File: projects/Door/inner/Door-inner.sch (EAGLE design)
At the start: 25 parts, among them IC1 7815T, IC2 317T, J3 LCD_4PIN, X1 POWERSUPPLY_DC21MMX, Y1 16MHz

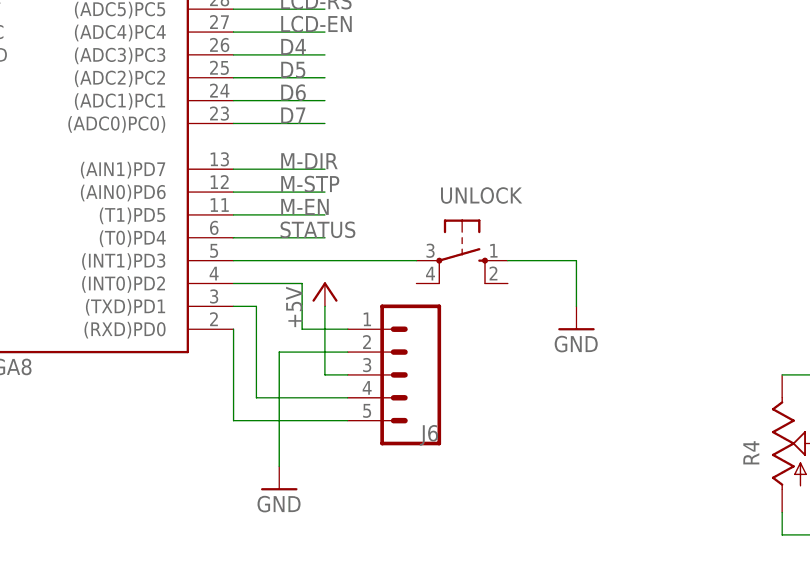
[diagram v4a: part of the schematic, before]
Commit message: New door, for making with plated through-holes
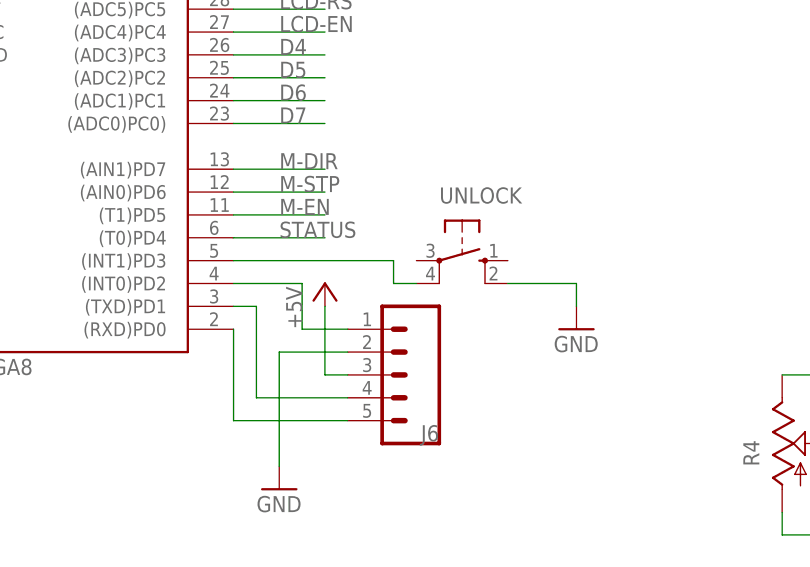
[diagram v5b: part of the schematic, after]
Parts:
- D1: device diode:DIODE-D-7.5 -> diode:DIODE-D-12.5
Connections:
- net GND: now also UNLOCK.S1; no longer UNLOCK.S
- net N$12: now also UNLOCK.P1; no longer UNLOCK.P
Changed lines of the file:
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@@
 <grid distance="0.1" unitdist="inch" unit="inch" style="lines" multiple="1" display="no" altdistance="0.01" altunitdist="inch" altunit="inch"/>
 <layers>
-<layer number="1" name="Top" color="4" fill="1" visible="no" active="no"/>
-<layer number="2" name="Route2" color="16" fill="1" visible="no" active="no"/>
-<layer number="3" name="Route3" color="17" fill="1" visible="no" active="no"/>
-<layer number="4" name="Route4" color="18" fill="1" visible="no" active="no"/>
-<layer number="5" name="Route5" color="19" fill="1" visible="no" active="no"/>
-<layer number="6" name="Route6" color="25" fill="1" visible="no" active="no"/>
-<layer number="7" name="Route7" color="26" fill="1" visible="no" active="no"/>
-<layer number="8" name="Route8" color="27" fill="1" visible="no" active="no"/>
-<layer number="9" name="Route9" color="28" fill="1" visible="no" active="no"/>
-<layer number="10" name="Route10" color="29" fill="1" visible="no" active="no"/>
-<layer number="11" name="Route11" color="30" fill="1" visible="no" active="no"/>
-<layer number="12" name="Route12" color="20" fill="1" visible="no" active="no"/>
-<layer number="13" name="Route13" color="21" fill="1" visible="no" active="no"/>
-<layer number="14" name="Route14" color="22" fill="1" visible="no" active="no"/>
-<layer number="15" name="Route15" color="23" fill="1" visible="no" active="no"/>
-<layer number="16" name="Bottom" color="1" fill="1" visible="no" active="no"/>
-<layer number="17" name="Pads" color="2" fill="1" visible="no" active="no"/>
-<layer number="18" name="Vias" color="2" fill="1" visible="no" active="no"/>
-<layer number="19" name="Unrouted" color="6" fill="1" visible="no" active="no"/>
-<layer number="20" name="Dimension" color="24" fill="1" visible="no" active="no"/>
-<layer number="21" name="tPlace" color="7" fill="1" visible="no" active="no"/>
-<layer number="22" name="bPlace" color="7" fill="1" visible="no" active="no"/>
-<layer number="23" name="tOrigins" color="15" fill="1" visible="no" active="no"/>
-<layer number="24" name="bOrigins" color="15" fill="1" visible="no" active="no"/>
-<layer number="25" name="tNames" color="7" fill="1" visible="no" active="no"/>
-<layer number="26" name="bNames" color="7" fill="1" visible="no" active="no"/>
-<layer number="27" name="tValues" color="7" fill="1" visible="no" active="no"/>
-<layer number="28" name="bValues" color="7" fill="1" visible="no" active="no"/>
+<layer number="1" name="Top" color="4" fill="1" visible="yes" active="no"/>
+<layer number="2" name="Route2" color="16" fill="1" visible="yes" active="no"/>
+<layer number="3" name="Route3" color="17" fill="1" visible="yes" active="no"/>
+<layer number="4" name="Route4" color="18" fill="1" visible="yes" active="no"/>
+<layer number="5" name="Route5" color="19" fill="1" visible="yes" active="no"/>
+<layer number="6" name="Route6" color="25" fill="1" visible="yes" active="no"/>
+<layer number="7" name="Route7" color="26" fill="1" visible="yes" active="no"/>
+<layer number="8" name="Route8" color="27" fill="1" visible="yes" active="no"/>
+<layer number="9" name="Route9" color="28" fill="1" visible="yes" active="no"/>
+<layer number="10" name="Route10" color="29" fill="1" visible="yes" active="no"/>
+<layer number="11" name="Route11" color="30" fill="1" visible="yes" active="no"/>
+<layer number="12" name="Route12" color="20" fill="1" visible="yes" active="no"/>
+<layer number="13" name="Route13" color="21" fill="1" visible="yes" active="no"/>
+<layer number="14" name="Route14" color="22" fill="1" visible="yes" active="no"/>
+<layer number="15" name="Route15" color="23" fill="1" visible="yes" active="no"/>
+<layer number="16" name="Bottom" color="1" fill="1" visible="yes" active="no"/>
+<layer number="17" name="Pads" color="2" fill="1" visible="yes" active="no"/>
+<layer number="18" name="Vias" color="2" fill="1" visible="yes" active="no"/>
+<layer number="19" name="Unrouted" color="6" fill="1" visible="yes" active="no"/>
+<layer number="20" name="Dimension" color="24" fill="1" visible="yes" active="no"/>
+<layer number="21" name="tPlace" color="7" fill="1" visible="yes" active="no"/>
+<layer number="22" name="bPlace" color="7" fill="1" visible="yes" active="no"/>
+<layer number="23" name="tOrigins" color="15" fill="1" visible="yes" active="no"/>
+<layer number="24" name="bOrigins" color="15" fill="1" visible="yes" active="no"/>
+<layer number="25" name="tNames" color="7" fill="1" visible="yes" active="no"/>
+<layer number="26" name="bNames" color="7" fill="1" visible="yes" active="no"/>
+<layer number="27" name="tValues" color="7" fill="1" visible="yes" active="no"/>
+<layer number="28" name="bValues" color="7" fill="1" visible="yes" active="no"/>
 <layer number="29" name="tStop" color="7" fill="3" visible="no" active="no"/>
 <layer number="30" name="bStop" color="7" fill="6" visible="no" active="no"/>
@@
 <layer number="35" name="tGlue" color="7" fill="4" visible="no" active="no"/>
 <layer number="36" name="bGlue" color="7" fill="5" visible="no" active="no"/>
-<layer number="37" name="tTest" color="7" fill="1" visible="no" active="no"/>
-<layer number="38" name="bTest" color="7" fill="1" visible="no" active="no"/>
+<layer number="37" name="tTest" color="7" fill="1" visible="yes" active="no"/>
+<layer number="38" name="bTest" color="7" fill="1" visible="yes" active="no"/>
 <layer number="39" name="tKeepout" color="4" fill="11" visible="no" active="no"/>
 <layer number="40" name="bKeepout" color="1" fill="11" visible="no" active="no"/>
@@
 <layer number="44" name="Drills" color="7" fill="1" visible="no" active="no"/>
 <layer number="45" name="Holes" color="7" fill="1" visible="no" active="no"/>
-<layer number="46" name="Milling" color="3" fill="1" visible="no" active="no"/>
-<layer number="47" name="Measures" color="7" fill="1" visible="no" active="no"/>
-<layer number="48" name="Document" color="7" fill="1" visible="no" active="no"/>
-<layer number="49" name="Reference" color="7" fill="1" visible="no" active="no"/>
-<layer number="50" name="dxf" color="7" fill="1" visible="no" active="no"/>
-<layer number="51" name="tDocu" color="7" fill="1" visible="no" active="no"/>
-<layer number="52" name="bDocu" color="7" fill="1" visible="no" active="no"/>
-<layer number="53" name="tGND_GNDA" color="7" fill="9" visible="no" active="no"/>
-<layer number="54" name="bGND_GNDA" color="1" fill="9" visible="no" active="no"/>
-<layer number="56" name="wert" color="7" fill="1" visible="no" active="no"/>
-<layer number="57" name="tCAD" color="7" fill="1" visible="no" active="no"/>
-<layer number="59" name="tCarbon" color="7" fill="1" visible="no" active="no"/>
-<layer number="60" name="bCarbon" color="7" fill="1" visible="no" active="no"/>
+<layer number="46" name="Milling" color="3" fill="1" visible="yes" active="no"/>
+<layer number="47" name="Measures" color="7" fill="1" visible="yes" active="no"/>
+<layer number="48" name="Document" color="7" fill="1" visible="yes" active="no"/>
+<layer number="49" name="Reference" color="7" fill="1" visible="yes" active="no"/>
+<layer number="50" name="dxf" color="7" fill="1" visible="yes" active="no"/>
+<layer number="51" name="tDocu" color="7" fill="1" visible="yes" active="no"/>
+<layer number="52" name="bDocu" color="7" fill="1" visible="yes" active="no"/>
+<layer number="53" name="tGND_GNDA" color="7" fill="9" visible="yes" active="no"/>
+<layer number="54" name="bGND_GNDA" color="1" fill="9" visible="yes" active="no"/>
+<layer number="56" name="wert" color="7" fill="1" visible="yes" active="no"/>
+<layer number="57" name="tCAD" color="7" fill="1" visible="yes" active="no"/>
+<layer number="59" name="tCarbon" color="7" fill="1" visible="yes" active="no"/>
+<layer number="60" name="bCarbon" color="7" fill="1" visible="yes" active="no"/>
 <layer number="88" name="SimResults" color="9" fill="1" visible="yes" active="yes"/>
 <layer number="89" name="SimProbes" color="9" fill="1" visible="yes" active="yes"/>
@@
 <part name="GND11" library="supply1" deviceset="GND" device=""/>
 <part name="GND19" library="supply1" deviceset="GND" device=""/>
-<part name="D1" library="diode" deviceset="DIODE-" device="D-7.5" value="M7"/>
+<part name="D1" library="diode" deviceset="DIODE-" device="D-12.5" value="M7"/>
 <part name="X1" library="SmartPrj" deviceset="POWERSUPPLY_DC21MM" device="X"/>
 <part name="P+8" library="supply1" deviceset="+5V" device=""/>
@@
 </segment>
 <segment>
-<pinref part="UNLOCK" gate="1" pin="S"/>
-<wire x1="139.7" y1="2.54" x2="147.32" y2="2.54" width="0.1524" layer="91"/>
-<wire x1="147.32" y1="2.54" x2="147.32" y2="-2.54" width="0.1524" layer="91"/>
 <pinref part="GND14" gate="1" pin="GND"/>
+<pinref part="UNLOCK" gate="1" pin="S1"/>
+<wire x1="147.32" y1="0" x2="147.32" y2="-2.54" width="0.1524" layer="91"/>
+<wire x1="139.7" y1="0" x2="147.32" y2="0" width="0.1524" layer="91"/>
 </segment>
 <segment>
@@
 <segment>
 <pinref part="ZIC1" gate="G$1" pin="(INT1)PD3"/>
-<pinref part="UNLOCK" gate="1" pin="P"/>
-<wire x1="109.22" y1="2.54" x2="129.54" y2="2.54" width="0.1524" layer="91"/>
-</segment>
-</net>
+<wire x1="109.22" y1="2.54" x2="127" y2="2.54" width="0.1524" layer="91"/>
+<pinref part="UNLOCK" gate="1" pin="P1"/>
+<wire x1="129.54" y1="0" x2="127" y2="0" width="0.1524" layer="91"/>
+<wire x1="127" y1="0" x2="127" y2="2.54" width="0.1524" layer="91"/>
+</segment>
+</net>
